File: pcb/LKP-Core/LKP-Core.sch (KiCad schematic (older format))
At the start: 34 parts, among them J1 Intercon L, J2 Intercon R, J3 Power JST PH, J4 IO, J5 SWD, J6 WS281x, U1 CY8C4246AZI-M445

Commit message: Derp
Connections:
- net E0_0: now also J1.17 (Pin_17), RN1.4 (R4.1); no longer J1.2 (Pin_2), RN6.1 (R1.1)
- net E0_1: now also J1.16 (Pin_16), RN1.3 (R3.1); no longer J1.3 (Pin_3), RN6.2 (R2.1)
- net E0_10: now also J1.7 (Pin_7), RN8.2 (R2.1); no longer J1.12 (Pin_12), RN4.3 (R3.1)
- net E0_11: now also J1.6 (Pin_6), RN8.1 (R1.1); no longer J1.13 (Pin_13), RN4.4 (R4.1)
- net E0_12: now also J1.5 (Pin_5), RN6.4 (R4.1); no longer J1.14 (Pin_14), RN1.1 (R1.1)
- net E0_13: now also J1.4 (Pin_4), RN6.3 (R3.1); no longer J1.15 (Pin_15), RN1.2 (R2.1)
- net E0_14: now also J1.3 (Pin_3), RN6.2 (R2.1); no longer J1.16 (Pin_16), RN1.3 (R3.1)
- net E0_15: now also J1.2 (Pin_2), RN6.1 (R1.1); no longer J1.17 (Pin_17), RN1.4 (R4.1)
- net E0_2: now also J1.15 (Pin_15), RN1.2 (R2.1); no longer J1.4 (Pin_4), RN6.3 (R3.1)
- net E0_3: now also J1.14 (Pin_14), RN1.1 (R1.1); no longer J1.5 (Pin_5), RN6.4 (R4.1)
- net E0_4: now also J1.13 (Pin_13), RN4.4 (R4.1); no longer J1.6 (Pin_6), RN8.1 (R1.1)
- net E0_5: now also J1.12 (Pin_12), RN4.3 (R3.1); no longer J1.7 (Pin_7), RN8.2 (R2.1)
- net E0_6: now also J1.11 (Pin_11), RN4.2 (R2.1); no longer J1.8 (Pin_8), RN8.3 (R3.1)
- net E0_7: now also J1.10 (Pin_10), RN4.1 (R1.1); no longer J1.9 (Pin_9), RN8.4 (R4.1)
- net E0_8: now also J1.9 (Pin_9), RN8.4 (R4.1); no longer J1.10 (Pin_10), RN4.1 (R1.1)
- net E0_9: now also J1.8 (Pin_8), RN8.3 (R3.1); no longer J1.11 (Pin_11), RN4.2 (R2.1)
- net S0_0: now also RN1.5 (R4.2), U1.45 (P0.6); no longer RN6.8 (R1.2), U1.22 (P3.4)
- net S0_1: now also RN1.6 (R3.2), U1.44 (P0.5); no longer RN6.7 (R2.2), U1.23 (P3.5)
- net S0_10: now also RN8.7 (R2.2), U1.32 (P4.5); no longer RN4.6 (R3.2), U1.40 (P0.1)
- net S0_11: now also RN8.8 (R1.2), U1.31 (P4.4); no longer RN4.5 (R4.2), U1.41 (P0.2)
- net S0_12: now also RN6.5 (R4.2), U1.25 (P3.7); no longer RN1.8 (R1.2), U1.42 (P0.3)
- net S0_13: now also RN6.6 (R3.2), U1.24 (P3.6); no longer RN1.7 (R2.2), U1.43 (P0.4)
- net S0_14: now also RN6.7 (R2.2), U1.23 (P3.5); no longer RN1.6 (R3.2), U1.44 (P0.5)
- net S0_15: now also RN6.8 (R1.2), U1.22 (P3.4); no longer RN1.5 (R4.2), U1.45 (P0.6)
- net S0_2: now also RN1.7 (R2.2), U1.43 (P0.4); no longer RN6.6 (R3.2), U1.24 (P3.6)
- net S0_3: now also RN1.8 (R1.2), U1.42 (P0.3); no longer RN6.5 (R4.2), U1.25 (P3.7)
- net S0_4: now also RN4.5 (R4.2), U1.41 (P0.2); no longer RN8.8 (R1.2), U1.31 (P4.4)
- net S0_5: now also RN4.6 (R3.2), U1.40 (P0.1); no longer RN8.7 (R2.2), U1.32 (P4.5)
- net S0_6: now also RN4.7 (R2.2), U1.39 (P0.0); no longer RN8.6 (R3.2), U1.33 (P4.6)
- net S0_7: now also RN4.8 (R1.2), U1.38 (P7.1); no longer RN8.5 (R4.2), U1.37 (P7.0)
- net S0_8: now also RN8.5 (R4.2), U1.37 (P7.0); no longer RN4.8 (R1.2), U1.38 (P7.1)
- net S0_9: now also RN8.6 (R3.2), U1.33 (P4.6); no longer RN4.7 (R2.2), U1.39 (P0.0)
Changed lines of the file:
@@
 	1    0    0    -1
 $EndComp
-Text Label 2050 3300 2    50   ~ 0
+Text Label 1050 4100 0    50   ~ 0
 E0_0
-Text Label 1050 3400 0    50   ~ 0
+Text Label 2050 4000 2    50   ~ 0
 E0_1
 Wire Wire Line
@@
 Wire Wire Line
 	1050 3400 1300 3400
-Text Label 2050 3400 2    50   ~ 0
+Text Label 1050 4000 0    50   ~ 0
 E0_2
-Text Label 1050 3500 0    50   ~ 0
+Text Label 2050 3900 2    50   ~ 0
 E0_3
 Wire Wire Line
@@
 Wire Wire Line
 	1050 3500 1300 3500
-Text Label 2050 3500 2    50   ~ 0
+Text Label 1050 3900 0    50   ~ 0
 E0_4
-Text Label 1050 3600 0    50   ~ 0
+Text Label 2050 3800 2    50   ~ 0
 E0_5
 Wire Wire Line
@@
 	1300 3600 1050 3600
 Text Label 3350 2800 0    50   ~ 0
-E0_12
+E0_3
 $Comp
 L Device:R_Pack04 RN1
@@
 	4200 2400 3950 2400
 Text Label 3950 2400 0    50   ~ 0
-E0_8
+E0_7
 Wire Wire Line
 	8250 5400 8000 5400
@@
 	8000 5100 8250 5100
 Text Label 8250 5400 2    50   ~ 0
-E0_7
+E0_8
 Text Label 8250 5300 2    50   ~ 0
-E0_6
+E0_9
 Text Label 8250 5200 2    50   ~ 0
-E0_5
+E0_10
 Text Label 8250 5100 2    50   ~ 0
-E0_4
+E0_11
 Wire Wire Line
 	6450 4000 6800 4000
@@
 S1_SH
 Text Label 6700 5400 2    50   ~ 0
-S0_7
+S0_8
 Wire Wire Line
 	6700 5100 6450 5100
@@
 	6450 3700 7150 3700
 Text Label 4600 2400 0    50   ~ 0
-S0_8
+S0_7
 $Comp
 L Device:R_Pack04 RN4
@@
 S0_SH
 Text Label 4600 3100 0    50   ~ 0
-S0_15
+S0_0
 Text Label 4600 3000 0    50   ~ 0
-S0_14
+S0_1
 Text Label 4600 2900 0    50   ~ 0
-S0_13
+S0_2
 Text Label 4600 2800 0    50   ~ 0
-S0_12
+S0_3
 Text Label 4600 2700 0    50   ~ 0
-S0_11
+S0_4
 Text Label 4600 2600 0    50   ~ 0
-S0_10
+S0_5
 Text Label 4600 2500 0    50   ~ 0
-S0_9
+S0_6
 Text Label 6700 5500 2    50   ~ 0
-S0_8
+S0_7
 Text Label 6700 4800 2    50   ~ 0
 S1_12
 Text Label 6700 4000 2    50   ~ 0
-S0_6
+S0_9
 Text Label 6700 3900 2    50   ~ 0
-S0_5
+S0_10
 Text Label 6700 3800 2    50   ~ 0
-S0_4
+S0_11
 Wire Wire Line
 	7350 3200 7100 3200
@@
 	7100 2900 7350 2900
 Text Label 7350 3200 2    50   ~ 0
-E0_3
+E0_12
 Text Label 7350 3100 2    50   ~ 0
-E0_2
+E0_13
 Text Label 7350 3000 2    50   ~ 0
-E0_1
+E0_14
 Text Label 7350 2900 2    50   ~ 0
-E0_0
+E0_15
 $Comp
 L Device:R_Pack04 RN6
@@
 	6450 2900 6700 2900
 Text Label 6700 3200 2    50   ~ 0
-S0_3
+S0_12
 Text Label 6700 3100 2    50   ~ 0
-S0_2
+S0_13
 Text Label 6700 3000 2    50   ~ 0
-S0_1
+S0_14
 Text Label 6700 2900 2    50   ~ 0
-S0_0
+S0_15
 $Comp
 L power:GND #PWR018
@@
 $EndComp
 Text Label 3350 2900 0    50   ~ 0
+E0_2
+Text Label 3350 3000 0    50   ~ 0
+E0_1
+Text Label 3350 3100 0    50   ~ 0
+E0_0
+Wire Wire Line
+	3350 2800 3600 2800
+Wire Wire Line
+	3600 2900 3350 2900
+Wire Wire Line
+	3350 3000 3600 3000
+Wire Wire Line
+	3600 3100 3350 3100
+Text Label 1050 3800 0    50   ~ 0
+E0_6
+Text Label 2050 3700 2    50   ~ 0
+E0_7
+Text Label 1050 3700 0    50   ~ 0
+E0_8
+Text Label 2050 3600 2    50   ~ 0
+E0_9
+Text Label 1050 3600 0    50   ~ 0
+E0_10
+Text Label 2050 3500 2    50   ~ 0
+E0_11
+Text Label 1050 3500 0    50   ~ 0
+E0_12
+Text Label 2050 3400 2    50   ~ 0
 E0_13
-Text Label 3350 3000 0    50   ~ 0
+Text Label 1050 3400 0    50   ~ 0
 E0_14
-Text Label 3350 3100 0    50   ~ 0
-E0_15
-Wire Wire Line
-	3350 2800 3600 2800
-Wire Wire Line
-	3600 2900 3350 2900
-Wire Wire Line
-	3350 3000 3600 3000
-Wire Wire Line
-	3600 3100 3350 3100
-Text Label 2050 3600 2    50   ~ 0
-E0_6
-Text Label 1050 3700 0    50   ~ 0
-E0_7
-Text Label 2050 3700 2    50   ~ 0
-E0_8
-Text Label 1050 3800 0    50   ~ 0
-E0_9
-Text Label 2050 3800 2    50   ~ 0
-E0_10
-Text Label 1050 3900 0    50   ~ 0
-E0_11
-Text Label 2050 3900 2    50   ~ 0
-E0_12
-Text Label 1050 4000 0    50   ~ 0
-E0_13
-Text Label 2050 4000 2    50   ~ 0
-E0_14
-Text Label 1050 4100 0    50   ~ 0
+Text Label 2050 3300 2    50   ~ 0
 E0_15
 Wire Wire Line
@@
 	4000 5000 4850 5000
 Text Label 3950 2500 0    50   ~ 0
-E0_9
+E0_6
 Text Label 3950 2600 0    50   ~ 0
-E0_10
+E0_5
 Wire Wire Line
 	3950 2500 4200 2500
@@
 	3950 2700 4200 2700
 Text Label 3950 2700 0    50   ~ 0
-E0_11
+E0_4
 Wire Wire Line
 	4000 2900 4850 2900

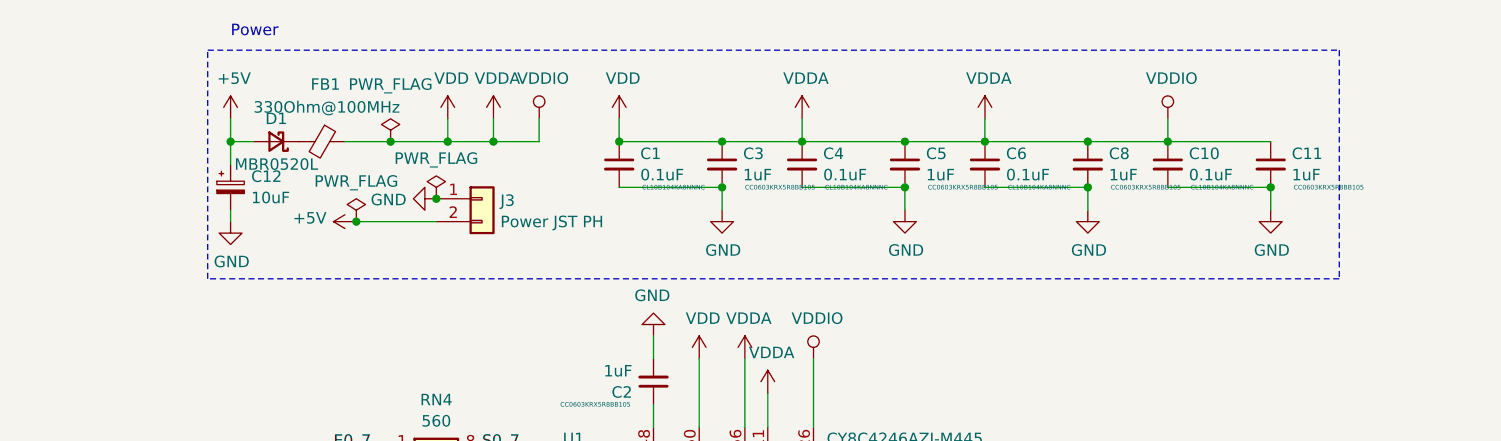
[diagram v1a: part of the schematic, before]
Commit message: Make reverse voltage protection also work with the tantalum filter cap.
Bump LKP-Core version number
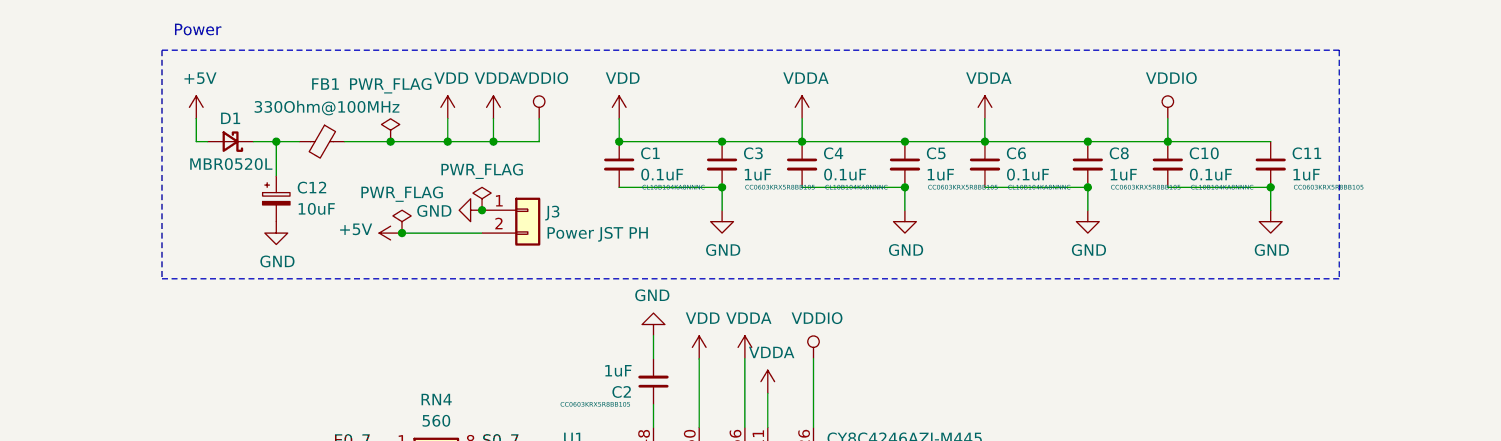
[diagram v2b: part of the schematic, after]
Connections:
- net +5V: no longer C12.1
- net at D1.1 (K), FB1.2: now also C12.1
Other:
- moved on the sheet: C12, D1, J3
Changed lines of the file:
@@
 EESchema Schematic File Version 4
-LIBS:LKP-Core-cache
-EELAYER 29 0
+EELAYER 30 0
 EELAYER END
 $Descr A4 11693 8268
@@
 Sheet 1 1
 Title "LKP-Core"
-Date ""
-Rev ""
-Comp ""
+Date "2020-09-26"
+Rev "v1.1"
+Comp "dogtopus"
 Comment1 ""
 Comment2 ""
@@
 L power:+5V #PWR03
 U 1 1 5D3DD54C
-P 3500 950
-F 0 "#PWR03" H 3500 800 50  0001 C CNN
-F 1 "+5V" H 3515 1126 50  0000 C CNN
-F 2 "" H 3500 950 50  0001 C CNN
-F 3 "" H 3500 950 50  0001 C CNN
-	1    3500 950
+P 3350 950
+F 0 "#PWR03" H 3350 800 50  0001 C CNN
+F 1 "+5V" H 3365 1126 50  0000 C CNN
+F 2 "" H 3350 950 50  0001 C CNN
+F 3 "" H 3350 950 50  0001 C CNN
+	1    3350 950
 	1    0    0    -1
 $EndComp
@@
 L Connector_Generic:Conn_01x02 J3
 U 1 1 5D59EA64
-P 4600 1300
-F 0 "J3" H 4680 1292 50  0000 L CNN
-F 1 "Power JST PH" H 4680 1199 50  0000 L CNN
-F 2 "Connector_JST:JST_PH_S2B-PH-SM4-TB_1x02-1MP_P2.00mm_Horizontal" H 4600 1300 50  0001 C CNN
-F 3 "~" H 4600 1300 50  0001 C CNN
-F 4 "Jellybean part." H 4600 1300 50  0001 C CNN "Comments"
-	1    4600 1300
+P 4800 1350
+F 0 "J3" H 4880 1342 50  0000 L CNN
+F 1 "Power JST PH" H 4880 1249 50  0000 L CNN
+F 2 "Connector_JST:JST_PH_S2B-PH-SM4-TB_1x02-1MP_P2.00mm_Horizontal" H 4800 1350 50  0001 C CNN
+F 3 "~" H 4800 1350 50  0001 C CNN
+F 4 "Jellybean part." H 4800 1350 50  0001 C CNN "Comments"
+	1    4800 1350
 	1    0    0    -1
 $EndComp
@@
 L power:GND #PWR04
 U 1 1 5D5A035E
-P 4400 1300
-F 0 "#PWR04" H 4400 1050 50  0001 C CNN
-F 1 "GND" V 4405 1170 50  0000 R CNN
-F 2 "" H 4400 1300 50  0001 C CNN
-F 3 "" H 4400 1300 50  0001 C CNN
-	1    4400 1300
+P 4600 1350
+F 0 "#PWR04" H 4600 1100 50  0001 C CNN
+F 1 "GND" V 4605 1220 50  0000 R CNN
+F 2 "" H 4600 1350 50  0001 C CNN
+F 3 "" H 4600 1350 50  0001 C CNN
+	1    4600 1350
 	0    1    1    0
 $EndComp
@@
 L power:+5V #PWR02
 U 1 1 5D5A13B9
-P 4050 1400
-F 0 "#PWR02" H 4050 1250 50  0001 C CNN
-F 1 "+5V" V 4065 1530 50  0000 L CNN
-F 2 "" H 4050 1400 50  0001 C CNN
-F 3 "" H 4050 1400 50  0001 C CNN
-	1    4050 1400
+P 4250 1450
+F 0 "#PWR02" H 4250 1300 50  0001 C CNN
+F 1 "+5V" V 4265 1580 50  0000 L CNN
+F 2 "" H 4250 1450 50  0001 C CNN
+F 3 "" H 4250 1450 50  0001 C CNN
+	1    4250 1450
 	0    -1   -1   0
 $EndComp
@@
 	4000 3100 4850 3100
 Wire Wire Line
-	3500 950  3500 1050
-Wire Wire Line
 	4000 1050 4200 1050
 Wire Wire Line
@@
 L power:PWR_FLAG #FLG02
 U 1 1 5D7706F5
-P 4400 1300
-F 0 "#FLG02" H 4400 1375 50  0001 C CNN
-F 1 "PWR_FLAG" H 4400 1476 50  0000 C CNN
-F 2 "" H 4400 1300 50  0001 C CNN
-F 3 "~" H 4400 1300 50  0001 C CNN
-	1    4400 1300
-	1    0    0    -1
-$EndComp
-Connection ~ 4400 1300
+P 4600 1350
+F 0 "#FLG02" H 4600 1425 50  0001 C CNN
+F 1 "PWR_FLAG" H 4600 1526 50  0000 C CNN
+F 2 "" H 4600 1350 50  0001 C CNN
+F 3 "~" H 4600 1350 50  0001 C CNN
+	1    4600 1350
+	1    0    0    -1
+$EndComp
+Connection ~ 4600 1350
 $Comp
 L power:PWR_FLAG #FLG01
 U 1 1 5D770DDD
-P 4050 1400
-F 0 "#FLG01" H 4050 1475 50  0001 C CNN
-F 1 "PWR_FLAG" H 4050 1576 50  0000 C CNN
-F 2 "" H 4050 1400 50  0001 C CNN
-F 3 "~" H 4050 1400 50  0001 C CNN
-	1    4050 1400
+P 4250 1450
+F 0 "#FLG01" H 4250 1525 50  0001 C CNN
+F 1 "PWR_FLAG" H 4250 1626 50  0000 C CNN
+F 2 "" H 4250 1450 50  0001 C CNN
+F 3 "~" H 4250 1450 50  0001 C CNN
+	1    4250 1450
 	1    0    0    -1
 $EndComp
@@
 Wire Notes Line
 	8350 650  8350 1650
-Wire Notes Line
-	8350 1650 3400 1650
-Wire Notes Line
-	3400 1650 3400 650
-Wire Notes Line
-	3400 650  8350 650
-Text Notes 3500 600  0    50   ~ 0
-Power
 Wire Notes Line
 	3250 4200 1000 4200
@@
 L Device:D_Schottky_Small D1
 U 1 1 5D93FA0B
-P 3700 1050
-F 0 "D1" H 3700 950 50  0000 C CNN
-F 1 "MBR0520L" H 3700 1150 50  0000 C CNN
-F 2 "Diode_SMD:D_SOD-123" V 3700 1050 50  0001 C CNN
-F 3 "~" V 3700 1050 50  0001 C CNN
-F 4 "MBR0520L" H 3700 1050 50  0001 C CNN "Part Number"
-	1    3700 1050
+P 3500 1050
+F 0 "D1" H 3500 950 50  0000 C CNN
+F 1 "MBR0520L" H 3500 1150 50  0000 C CNN
+F 2 "Diode_SMD:D_SOD-123" V 3500 1050 50  0001 C CNN
+F 3 "~" V 3500 1050 50  0001 C CNN
+F 4 "MBR0520L" H 3500 1050 50  0001 C CNN "Part Number"
+	1    3500 1050
 	-1   0    0    1
 $EndComp
@@
 	4450 1050 4650 1050
 Wire Wire Line
-	3600 1050 3500 1050
-Wire Wire Line
-	4400 1400 4050 1400
-Connection ~ 4050 1400
+	4600 1450 4250 1450
+Connection ~ 4250 1450
 NoConn ~ 4850 4000
 Wire Wire Line
@@
 L Device:CP_Small C12
 U 1 1 5D5BF537
-P 3500 1250
-F 0 "C12" H 3590 1297 50  0000 L CNN
-F 1 "10uF" H 3590 1204 50  0000 L CNN
-F 2 "Capacitor_Tantalum_SMD:CP_EIA-3216-18_Kemet-A" H 3500 1250 50  0001 C CNN
-F 3 "~" H 3500 1250 50  0001 C CNN
-	1    3500 1250
-	1    0    0    -1
-$EndComp
-Wire Wire Line
-	3500 1050 3500 1150
-Connection ~ 3500 1050
+P 3700 1300
+F 0 "C12" H 3790 1347 50  0000 L CNN
+F 1 "10uF" H 3790 1254 50  0000 L CNN
+F 2 "Capacitor_Tantalum_SMD:CP_EIA-3216-18_Kemet-A" H 3700 1300 50  0001 C CNN
+F 3 "~" H 3700 1300 50  0001 C CNN
+	1    3700 1300
+	1    0    0    -1
+$EndComp
 $Comp
 L power:GND #PWR01
 U 1 1 5D5CE4B4
-P 3500 1400
-F 0 "#PWR01" H 3500 1150 50  0001 C CNN
-F 1 "GND" H 3505 1224 50  0000 C CNN
-F 2 "" H 3500 1400 50  0001 C CNN
-F 3 "" H 3500 1400 50  0001 C CNN
-	1    3500 1400
-	1    0    0    -1
-$EndComp
-Wire Wire Line
-	3500 1350 3500 1400
+P 3700 1400
+F 0 "#PWR01" H 3700 1150 50  0001 C CNN
+F 1 "GND" H 3705 1224 50  0000 C CNN
+F 2 "" H 3700 1400 50  0001 C CNN
+F 3 "" H 3700 1400 50  0001 C CNN
+	1    3700 1400
+	1    0    0    -1
+$EndComp
+Wire Wire Line
+	3600 1050 3700 1050
+Wire Wire Line
+	3700 1200 3700 1050
+Connection ~ 3700 1050
+Wire Wire Line
+	3700 1050 3800 1050
+Wire Wire Line
+	3350 950  3350 1050
+Wire Wire Line
+	3350 1050 3400 1050
+Wire Notes Line
+	8350 650  3200 650
+Wire Notes Line
+	3200 650  3200 1650
+Wire Notes Line
+	3200 1650 8350 1650
+Text Notes 3250 600  0    50   ~ 0
+Power
 $EndSCHEMATC

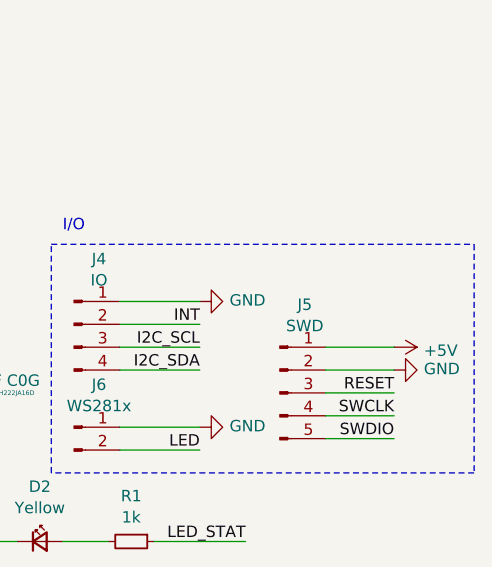
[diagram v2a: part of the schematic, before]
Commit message: Add info about LKP-IF-Qwiic. Add pin mapping table.
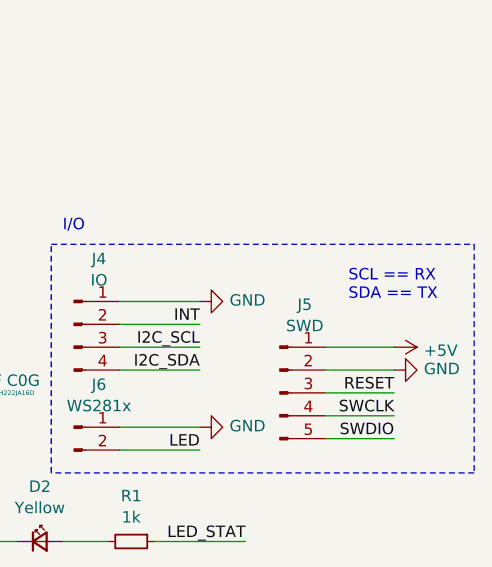
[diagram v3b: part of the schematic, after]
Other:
- note added: "SCL == RX\nSDA == TX"
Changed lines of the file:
@@
 Text Notes 3250 600  0    50   ~ 0
 Power
+Text Notes 9500 3400 0    50   ~ 0
+SCL == RX\nSDA == TX
 $EndSCHEMATC
